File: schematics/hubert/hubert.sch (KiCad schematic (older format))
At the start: 3 parts, among them U1 nRF52840

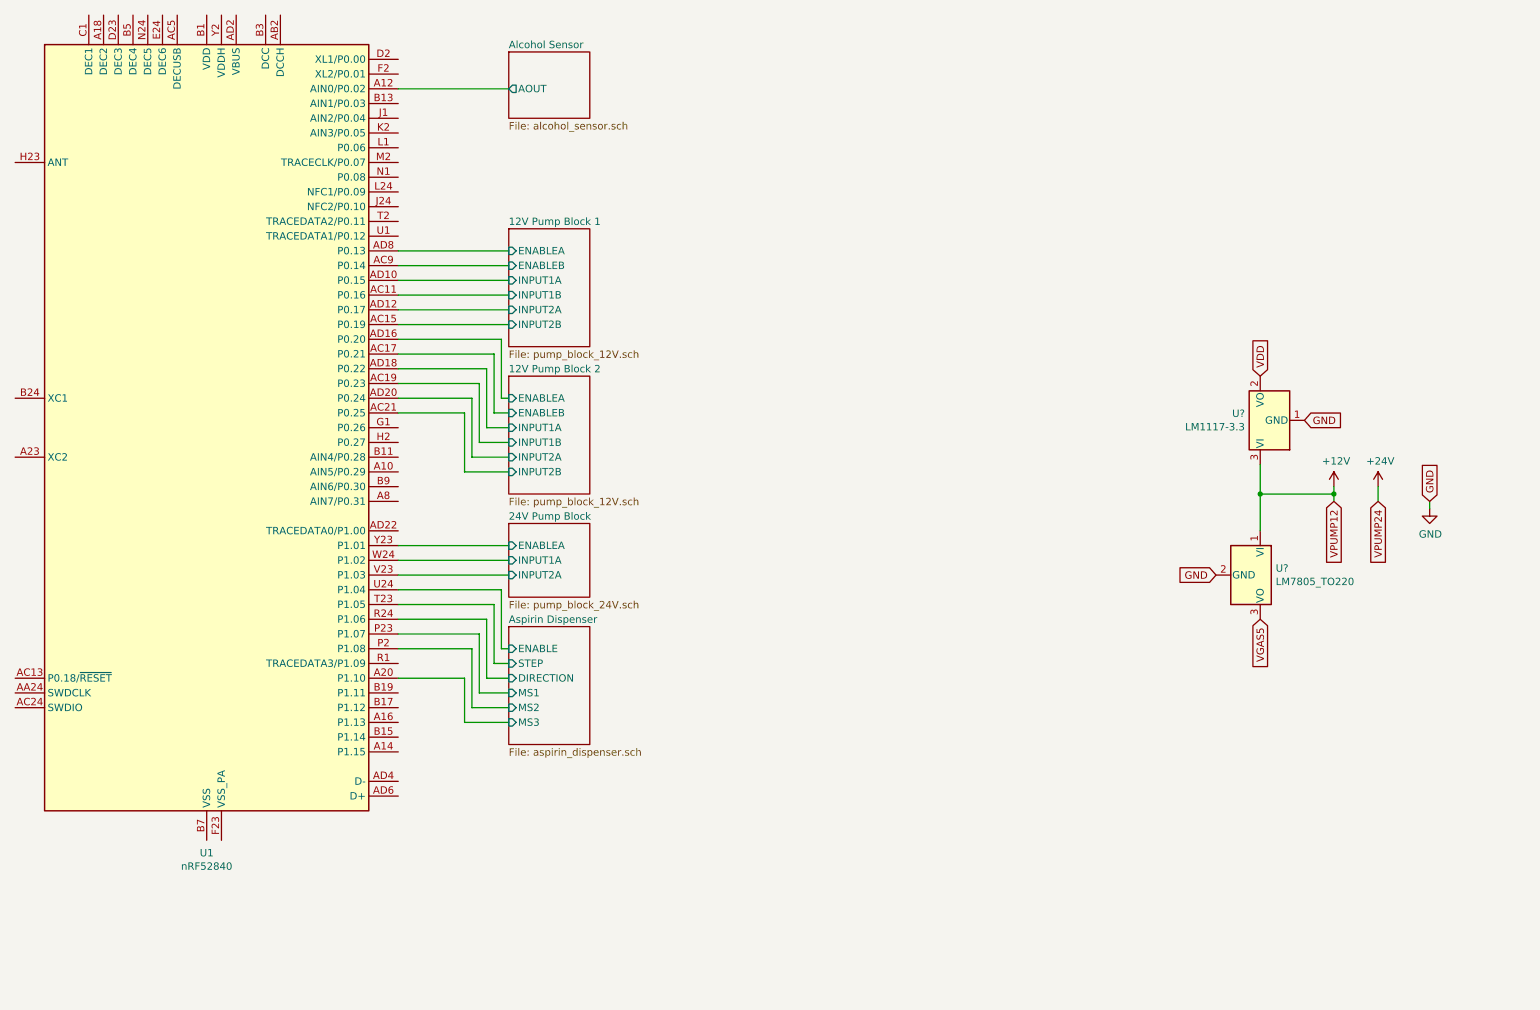
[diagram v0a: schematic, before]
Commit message: updated schematics
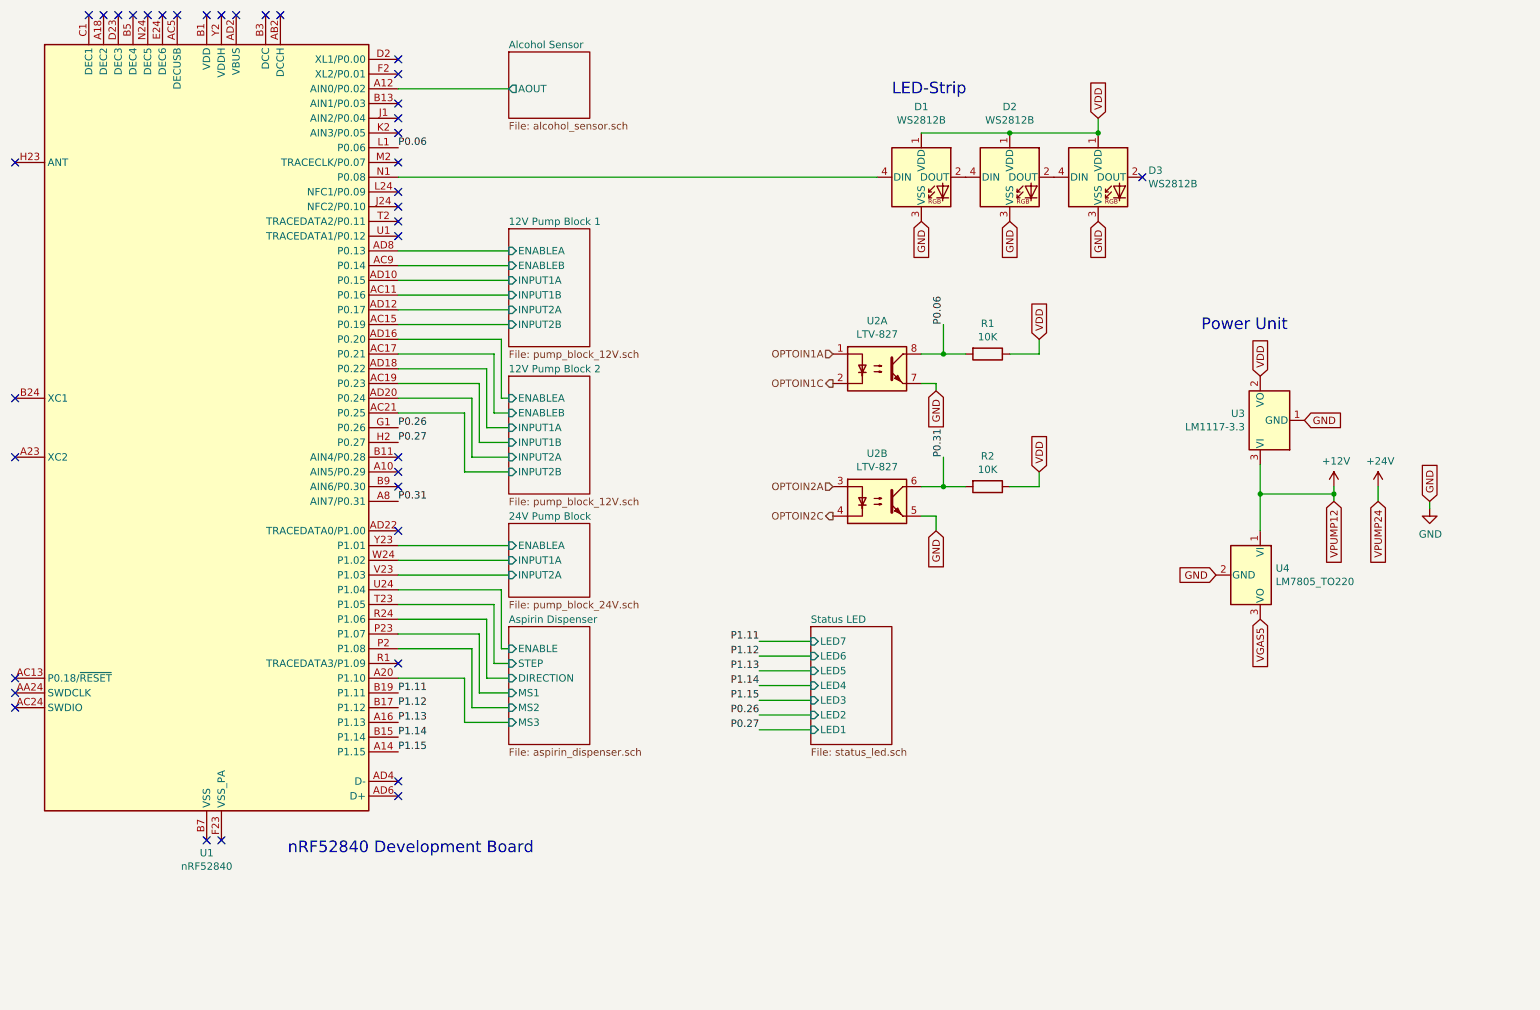
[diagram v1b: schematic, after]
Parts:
- added D1, D2, D3: WS2812B, LED_SMD:LED_WS2812B_PLCC4_5.0x5.0mm_P3.2mm, symbol LED:WS2812B
- added R1, R2: 10K, symbol Device:R
- added U2: LTV-827, Package_DIP:DIP-8_W7.62mm, symbol Isolator:LTV-827
- gave numbers to parts that had none: 2
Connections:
- net GND: now also D1.3 (VSS), D2.3 (VSS), D3.3 (VSS), U2.5, U2.7
- net VDD: now also D1.1 (VDD), D2.1 (VDD), D3.1 (VDD), R1.1, R2.1
- net P1.15: now reaches U1.A14 (P1.15)
- net P1.13: now reaches U1.A16 (P1.13)
- net P0.31: now reaches U1.A8 (AIN7/P0.31)
- net P0.31: now also R2.2, U2.6
- net P1.14: now reaches U1.B15 (P1.14)
- net P1.12: now reaches U1.B17 (P1.12)
- net P1.11: now reaches U1.B19 (P1.11)
- net P0.26: now reaches U1.G1 (P0.26)
- net P0.27: now reaches U1.H2 (P0.27)
- net P0.06: now reaches U1.L1 (P0.06)
- net P0.06: now also R1.2, U2.8
- net at U1.N1 (P0.08): now also D1.4 (DIN)
- new net: D1.2 (DOUT), D2.4 (DIN)
- new net: D2.2 (DOUT), D3.4 (DIN)
- new net OPTOIN1A: U2.1
- new net OPTOIN1C: U2.2
- new net OPTOIN2A: U2.3
- new net OPTOIN2C: U2.4
- no-connect marks 0 -> 38
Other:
- note added: "LED-Strip"
- note added: "Power Unit"
- note added: "nRF52840 Development Board"

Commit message: fixed ERC problems and added connector for input pins
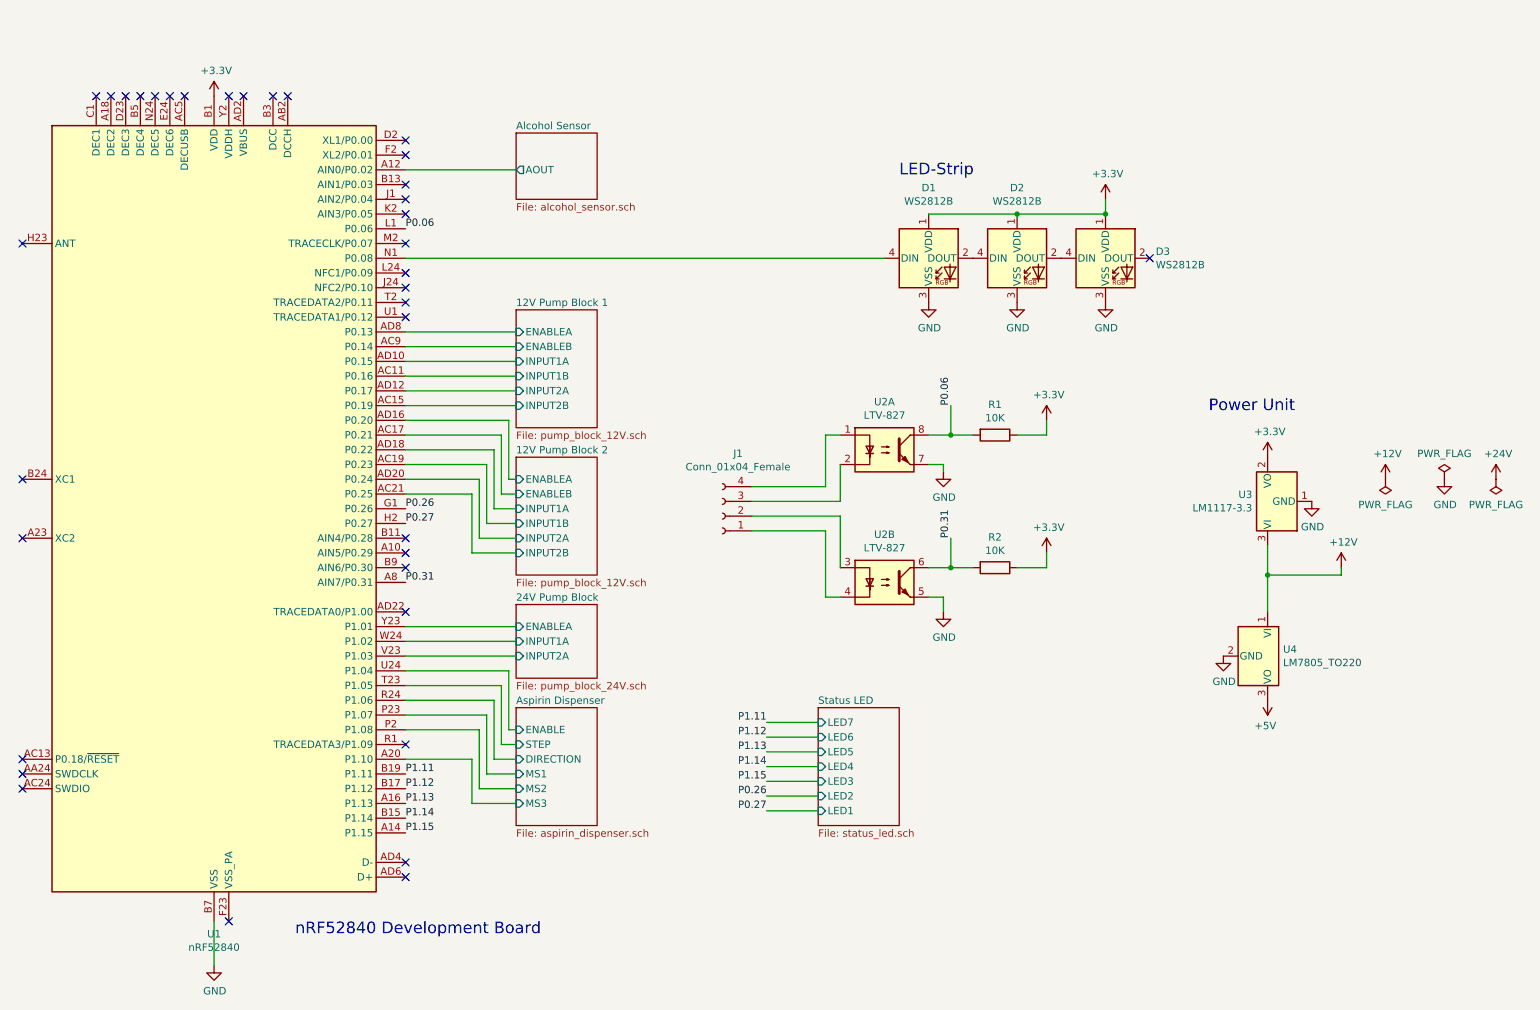
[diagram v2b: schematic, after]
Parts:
- added J1: Conn_01x04_Female, symbol Connector:Conn_01x04_Female
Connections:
- net VDD is gone; now on net +3V3: D1.1 (VDD), D2.1 (VDD), D3.1 (VDD), R1.1, R2.1, U3.2 (VO)
- net GND: now also U1.B7 (VSS), U1.EP (VSS)
- net +3V3: now reaches U1.A22 (VDD), U1.AD14 (VDD), U1.AD23 (VDD), U1.B1 (VDD), U1.W1 (VDD)
- net OPTOIN1A: no longer names the net of U2.1
- net OPTOIN1A: now also J1.4 (Pin_4)
- net OPTOIN1C: no longer names the net of U2.2
- net OPTOIN1C: now also J1.3 (Pin_3)
- net OPTOIN2A: no longer names the net of U2.3
- net OPTOIN2A: now also J1.2 (Pin_2)
- net OPTOIN2C: no longer names the net of U2.4
- net OPTOIN2C: now also J1.1 (Pin_1)
- net VGAS5 renamed +5V
- no-connect marks 38 -> 36
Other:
- moved on the sheet: D1, D2, D3, R1, R2, U1, U2A, U2B, U3, U4

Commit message: started working on layout
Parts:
- J1: footprint (none) -> Connector_PinHeader_2.54mm:PinHeader_1x04_P2.54mm_Horizontal
- R1, R2: footprint (none) -> Resistor_THT:R_Axial_DIN0617_L17.0mm_D6.0mm_P25.40mm_Horizontal
- U3: footprint (none) -> Package_TO_SOT_THT:TO-220-3_Vertical
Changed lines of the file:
@@
 Sheet 1 7
 Title "Hubert"
-Date "2018-11-02"
-Rev "1.1"
+Date "2018-11-05"
+Rev "1.2"
 Comp ""
 Comment1 ""
@@
 F 0 "U3" V 9246 4004 50  0000 L CNN
 F 1 "LM1117-3.3" V 9155 4004 50  0000 L CNN
-F 2 "" H 9200 3900 50  0001 C CNN
+F 2 "Package_TO_SOT_THT:TO-220-3_Vertical" H 9200 3900 50  0001 C CNN
 F 3 "http://www.ti.com/lit/ds/symlink/lm1117.pdf" H 9200 3900 50  0001 C CNN
 	1    9200 3900
@@
 F 0 "R1" V 7143 3450 50  0000 C CNN
 F 1 "10K" V 7234 3450 50  0000 C CNN
-F 2 "" V 7280 3450 50  0001 C CNN
+F 2 "Resistor_THT:R_Axial_DIN0617_L17.0mm_D6.0mm_P25.40mm_Horizontal" V 7280 3450 50  0001 C CNN
 F 3 "~" H 7350 3450 50  0001 C CNN
 	1    7350 3450
@@
 F 0 "R2" V 7143 4350 50  0000 C CNN
 F 1 "10K" V 7234 4350 50  0000 C CNN
-F 2 "" V 7280 4350 50  0001 C CNN
+F 2 "Resistor_THT:R_Axial_DIN0617_L17.0mm_D6.0mm_P25.40mm_Horizontal" V 7280 4350 50  0001 C CNN
 F 3 "~" H 7350 4350 50  0001 C CNN
 	1    7350 4350
@@
 F 0 "J1" H 5394 3575 50  0000 C CNN
 F 1 "Conn_01x04_Female" H 5394 3666 50  0000 C CNN
-F 2 "" H 5500 4000 50  0001 C CNN
+F 2 "Connector_PinHeader_2.54mm:PinHeader_1x04_P2.54mm_Horizontal" H 5500 4000 50  0001 C CNN
 F 3 "~" H 5500 4000 50  0001 C CNN
 	1    5500 4000
